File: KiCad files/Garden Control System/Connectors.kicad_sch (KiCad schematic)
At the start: 4 parts, among them J1 Debug, J2 USB_C_Receptacle_USB2.0

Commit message: Close to finishing ethernet side
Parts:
- renumbered J1 to J3, J2 to J4, R1 to R4, R1 to R5
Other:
- moved on the sheet: J4, R4, R5

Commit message: working on power arch
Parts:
- added J2, J5, J6, J7: PJ-102AH, PJ-102AH:CUI_PJ-102AH, symbol PJ-102AH:PJ-102AH
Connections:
- net GND: now also J2.2, J2.3, J5.2, J5.3, J6.2, J6.3, J7.2, J7.3
- net VBUS renamed USB_VBUS
- new net M0_IN: J5.1
- new net M1_IN: J6.1
- new net M2_IN: J7.1
- new net VBAT: J2.1
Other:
- note added: "Pump/Fan supplies"

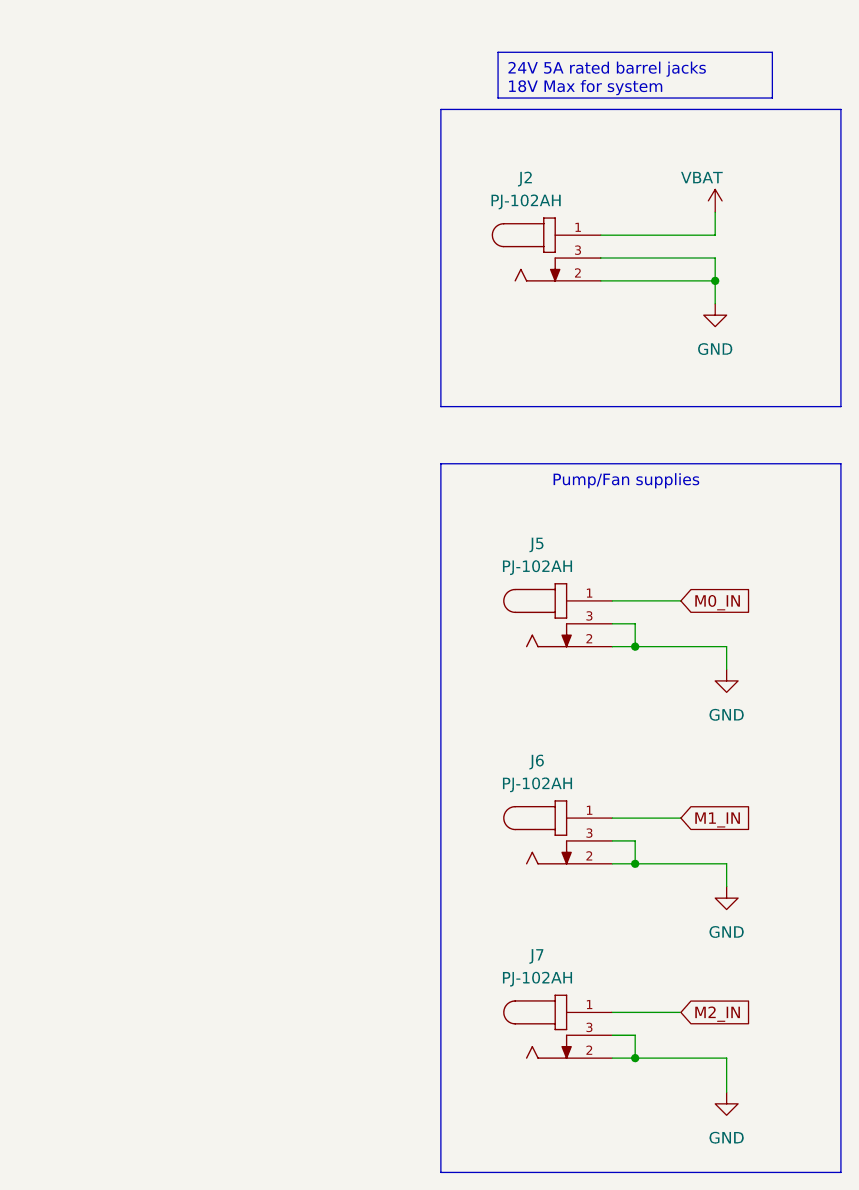
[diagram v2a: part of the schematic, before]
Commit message: expanded power supply section. completed LSD design. sized shunt resistors
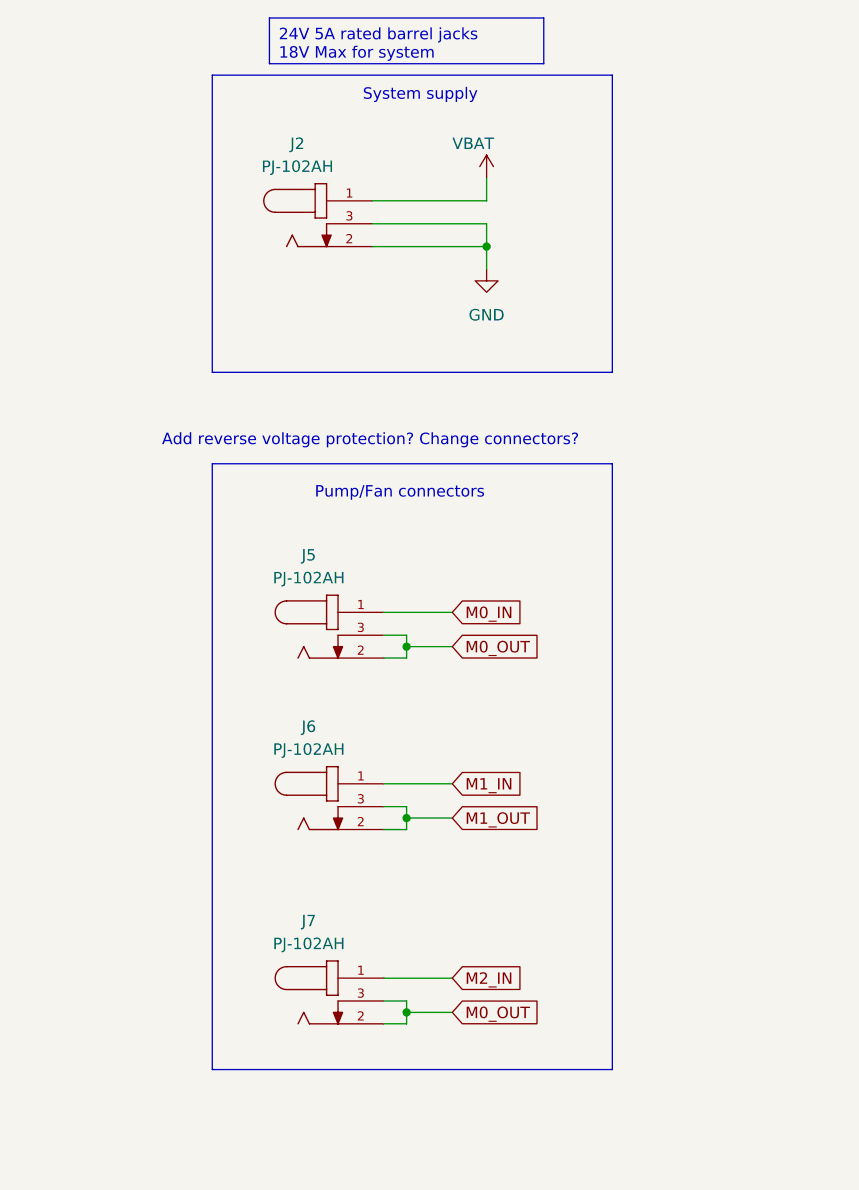
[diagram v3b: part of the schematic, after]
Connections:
- net GND: no longer J5.2, J5.3, J6.2, J6.3, J7.2, J7.3
- new net M0_OUT: J5.2, J5.3, J7.2, J7.3
- new net M1_OUT: J6.2, J6.3
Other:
- note added: "Add reverse voltage protection? Change connectors?"
- note added: "Pump/Fan connectors"
- note added: "System supply"
- note removed: "Pump/Fan supplies"
- moved on the sheet: J2, J5, J6, J7

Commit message: adding recent schematic progress
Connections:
- net +3.3V renamed 3V3
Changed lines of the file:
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@@
+		)
+	)
+	(text_box "OTG_FS Peripheral only setup, no Vbus sense."
+		(exclude_from_sim no)
+		(at 139.7 25.4 0)
+		(size 46.99 5.08)
+		(stroke
+			(width 0)
+			(type default)
+		)
+		(fill
+			(type color)
+			(color 255 255 194 1)
+		)
+		(effects
+			(font
+				(size 1.27 1.27)
+			)
+			(justify left top)
 		)
 	)
@@
 			)
 		)
-		(property "Value" "+3.3V"
-			(at 33.02 31.75 0)
-			(effects
-				(font
-					(size 1.27 1.27)
-				)
-			)
-		)
+		(property "Value" "3V3"
+			(at 35.56 35.5599 0)
+			(effects
+				(font
+					(size 1.27 1.27)
+				)
+				(justify left)
+			)
+		)

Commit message: we cookin' again. Added LSD and start temp sense section.
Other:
- note added: "Change this connector to pins Cap on NRST to avoid reset on interferance?"
- note added: "JTAG"
- note added: "Pump/Fan"
- note added: "System Supply"
- note added: "UART"
- note added: "USB"
- note removed: "Add TVS diodes for protection? ESD Caps? Cap on NRST to avoid reset on interferance?"
- note removed: "Add reverse voltage protection? Change connectors?"
- note removed: "Pump/Fan connectors"
- note removed: "System supply"
- moved on the sheet: J2, J3, J4, J5, J6, J7, R4, R5
